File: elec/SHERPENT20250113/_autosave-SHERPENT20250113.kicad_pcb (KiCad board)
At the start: 4 copper layers, 130.2 x 68.2 mm, 125 parts, among them J1 2137160001, J2 Conn_01x03_Socket, J3 Conn_01x03_Socket, Q1 NMOS, Q2 PMOS, Q3 NMOS, Q4 PMOS, SW1 CT1102, SW2 SW_Push, U1 MCP73831T-2ACI_OT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

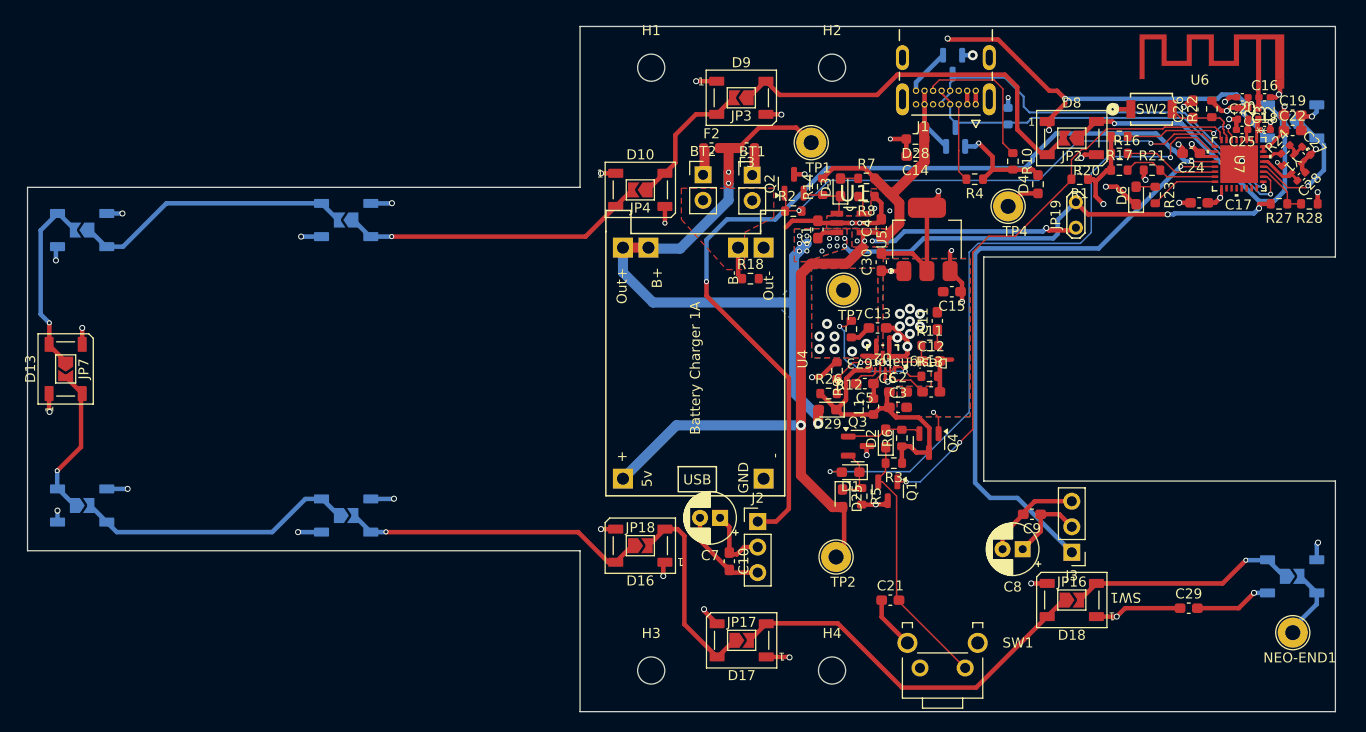
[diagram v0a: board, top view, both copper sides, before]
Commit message: b- != gnd
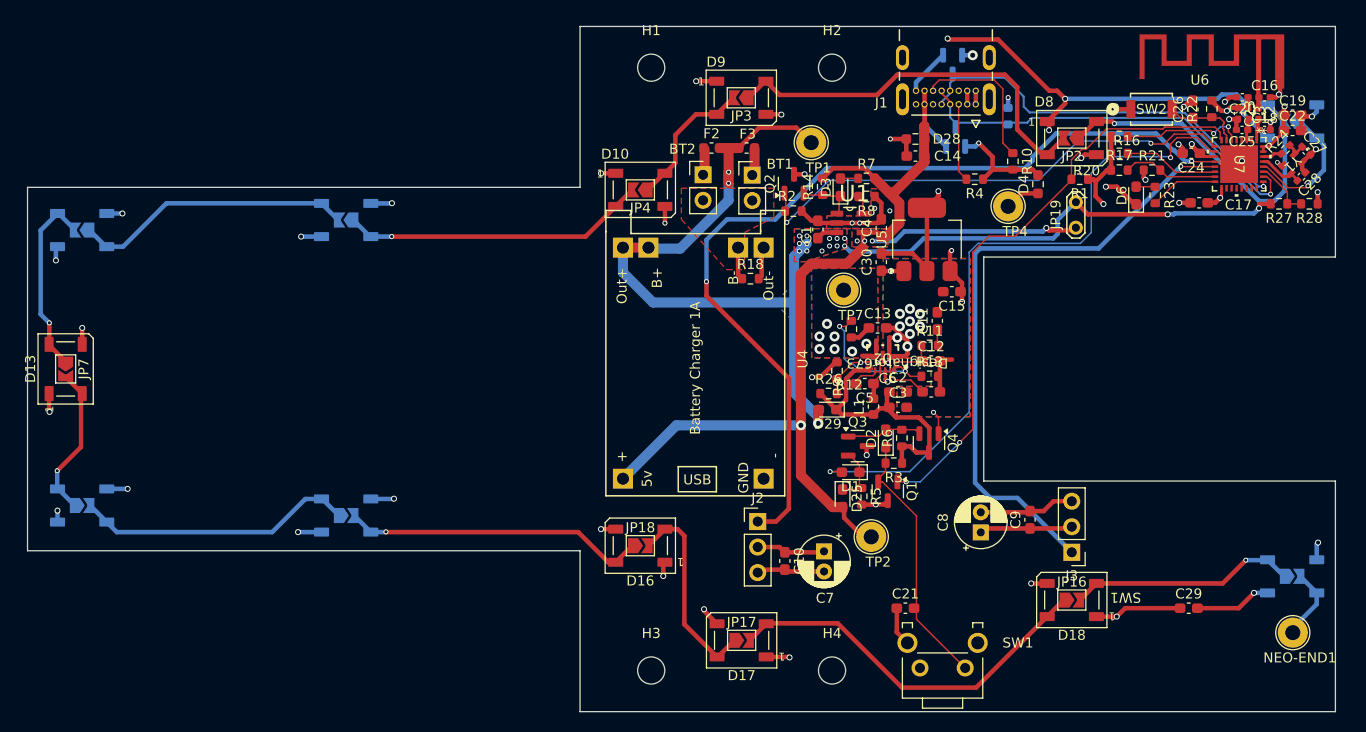
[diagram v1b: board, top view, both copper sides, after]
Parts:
- moved C7 10.9 mm to (156.2, 121.1), turned to -90 degrees
- moved C10 5.53 mm to (152.3, 122.1)
- moved C8 4.50 mm to (171.8, 119.3), turned to 90 degrees
- moved TP2 4.03 mm to (160.9, 119.7)
- moved C21 1.70 mm to (164.3, 126.8)
- moved C9 0.58 mm to (176.7, 118.0), turned to 90 degrees
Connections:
- D29 pad 2: /VBAT_LOAD -> /VBATT
- JP19 pad 2: /VBAT_LOAD -> /VBATT
- R27 pad 2: /VBAT_LOAD -> /VBATT
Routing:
- net /VBATT: track 72.1 -> 118.6 mm, vias 16 -> 18
- net /VBAT_LOAD: track 46.5 -> 0.00 mm, vias 2 -> 0
- net GND: track 140.3 -> 138.0 mm
- net /CHARGE: track 48.3 -> 49.9 mm
- net +9V: track 109.5 -> 110.8 mm
- net /VUSB: track 129.3 -> 128.2 mm
- removed copper zone on B.Cu, net /VBAT_LOAD
